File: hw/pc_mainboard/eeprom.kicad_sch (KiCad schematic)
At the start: 0 parts

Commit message: EEPROM Research (#36)
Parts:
- added CR1: eeprom_M24C02-WMN6TP, SO-8_STM, symbol pc_mainboard:eeprom_M24C02-WMN6TP
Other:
- title: (none) -> EEPROM
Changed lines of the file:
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@@
 	(generator_version "8.0")
 	(paper "A4")
+	(title_block
+		(title "EEPROM")
+	)
+	(symbol
+		(lib_id "pc_mainboard:eeprom_M24C02-WMN6TP")
+		(at 124.46 93.98 0)
+		(unit 1)
+		(exclude_from_sim no)
+		(in_bom yes)
+		(on_board yes)
+		(dnp no)
+		(fields_autoplaced yes)
+		(property "Reference" "CR1"
+			(at 144.78 83.82 0)
+			(effects
+				(font
+					(size 1.524 1.524)
+				)
+			)
+		)
+		(property "Value" "eeprom_M24C02-WMN6TP"
+			(at 144.78 86.36 0)
+			(effects
+				(font
+					(size 1.524 1.524)
+				)
+			)
+		)
+		(property "Footprint" "SO-8_STM"
+			(at 124.46 93.98 0)
+			(effects
+				(font
+					(size 1.27 1.27)
+					(italic yes)
+				)
+				(hide yes)
+			)
+		)
+		(property "Datasheet" "M24C02-WMN6TP"
+			(at 124.46 93.98 0)
+			(effects
+				(font
+					(size 1.27 1.27)
+					(italic yes)
+				)
+				(hide yes)
+			)
+		)
+		(property "Description" ""
+			(at 124.46 93.98 0)
+			(effects
+				(font
+					(size 1.27 1.27)
+				)
+				(hide yes)
+			)
+		)
+		(pin "1"
+		)
+		(pin "6"
+		)
+		(pin "3"
+		)
+		(pin "2"
+		)
+		(pin "7"
+		)
+		(pin "8"
+		)
+		(pin "5"
+		)
+		(pin "4"
+		)
+		(instances
+			(project ""
+				(path "/69a74940-cd00-4a75-bd5b-2bda9e86219a/0c2f5e6a-3e36-4818-980c-c86701037833"
+					(reference "CR1")
+					(unit 1)
+				)
+			)
+		)
+	)
 )

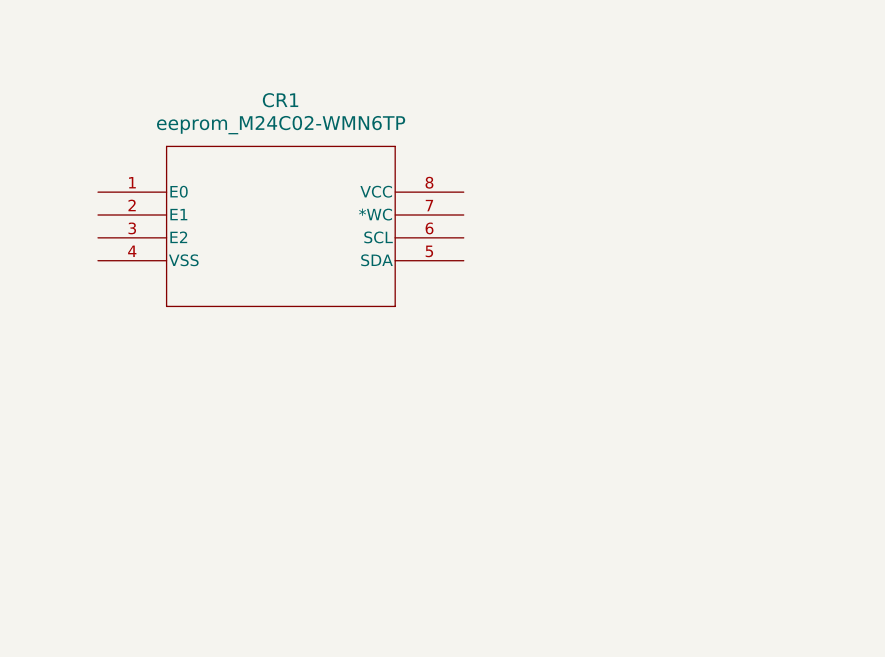
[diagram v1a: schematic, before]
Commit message: eeprom schematic, partial layout
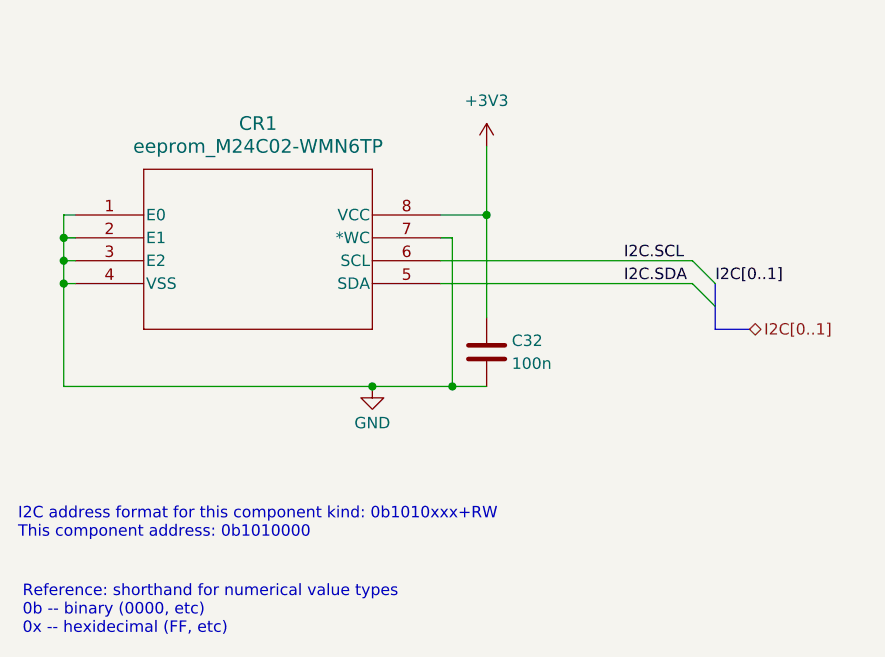
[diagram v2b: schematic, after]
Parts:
- added C32: 100n, Capacitor_SMD:C_0603_1608Metric, symbol Device:C
- CR1: footprint SO-8_STM -> pc_mainboard:eeprom_SO-8_STM
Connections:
- net GND: now reaches CR1.1 (E0)
- net GND: now also CR1.2 (E1), CR1.3 (E2), CR1.4 (VSS), CR1.7 (*WC), C32.2
- net I2C.SDA: now reaches CR1.5 (SDA)
- net I2C.SCL: now reaches CR1.6 (SCL)
- net +3V3: now reaches CR1.8 (VCC)
- net +3V3: now also C32.1
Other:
- note added: "I2C address format for this component kind: 0b1010xxx+RW This component address: 0b1010000"
- note added: "Reference: shorthand for numerical value types 0b -- binary (0000, etc) 0x -- hexidecimal (FF, etc)"
- moved on the sheet: CR1

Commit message: cleanup eeprom schematic format: removed crossed wires and localized endpoints
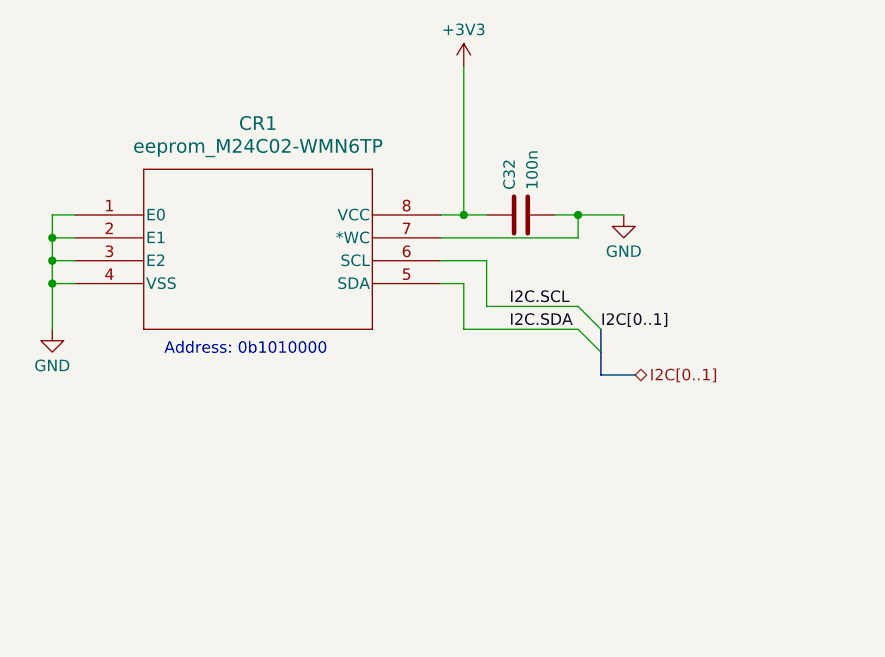
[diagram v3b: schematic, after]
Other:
- note added: "Address: 0b1010000"
- note removed: "I2C address format for this component kind: 0b1010xxx+RW This component address: 0b1010000"
- note removed: "Reference: shorthand for numerical value types 0b -- binary (0000, etc) 0x -- hexidecimal (FF, etc)"
- moved on the sheet: C32
